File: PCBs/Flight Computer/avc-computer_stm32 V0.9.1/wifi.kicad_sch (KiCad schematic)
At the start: 1 part, among them J3 ESP_01_Socket

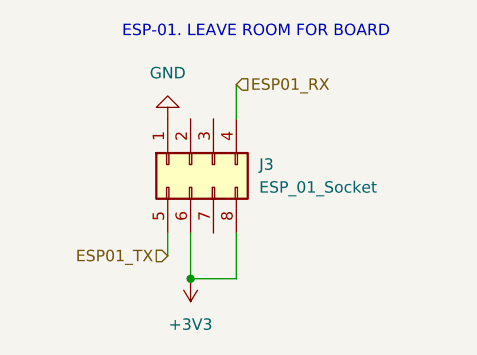
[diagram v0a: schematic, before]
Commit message: Fixed all issues except for 5v buck inductor heating
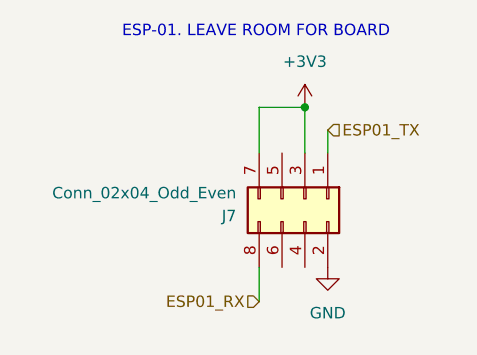
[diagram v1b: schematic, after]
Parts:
- removed J3: ESP_01_Socket, Connector_PinHeader_2.54mm:PinHeader_2x04_P2.54mm_Vertical, symbol Connector_Generic:Conn_02x04_Top_Bottom
- added J7: Conn_02x04_Odd_Even, Connector_PinHeader_2.54mm:PinHeader_2x04_P2.54mm_Vertical, symbol Connector_Generic:Conn_02x04_Odd_Even
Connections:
- net +3V3: now also J7.3 (Pin_3), J7.7 (Pin_7)
- net ESP01_RX: now also J7.8 (Pin_8)
- net ESP01_TX: now also J7.1 (Pin_1)
- net GND: now also J7.2 (Pin_2)
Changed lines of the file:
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@@
-(kicad_sch (version 20211123) (generator eeschema)
+(kicad_sch (version 20230121) (generator eeschema)
   (paper "A4")
-  (junction (at 124.46 74.93) (diameter 0) (color 0 0 0 0)
+  (junction (at 137.16 55.88) (diameter 0) (color 0 0 0 0)
   )
-  (wire (pts (xy 121.92 69.85) (xy 121.92 72.39))
-    (stroke (width 0) (type default) (color 0 0 0 0))
+  (wire (pts (xy 132.08 77.47) (xy 132.08 73.66))
+    (stroke (width 0) (type default))
   )
-  (wire (pts (xy 129.54 74.93) (xy 129.54 69.85))
-    (stroke (width 0) (type default) (color 0 0 0 0))
+  (wire (pts (xy 137.16 55.88) (xy 137.16 60.96))
+    (stroke (width 0) (type default))
   )
-  (wire (pts (xy 124.46 74.93) (xy 124.46 69.85))
-    (stroke (width 0) (type default) (color 0 0 0 0))
+  (wire (pts (xy 139.7 60.96) (xy 139.7 58.42))
+    (stroke (width 0) (type default))
   )
-  (wire (pts (xy 129.54 74.93) (xy 124.46 74.93))
-    (stroke (width 0) (type default) (color 0 0 0 0))
+  (wire (pts (xy 132.08 55.88) (xy 137.16 55.88))
+    (stroke (width 0) (type default))
   )
-  (wire (pts (xy 129.54 53.34) (xy 129.54 57.15))
-    (stroke (width 0) (type default) (color 0 0 0 0))
+  (wire (pts (xy 132.08 55.88) (xy 132.08 60.96))
+    (stroke (width 0) (type default))
   )
   (text "ESP-01. LEAVE ROOM FOR BOARD" (at 116.84 48.26 0)
     (effects (font (size 1.27 1.27)) (justify left bottom))
   )
-  (hierarchical_label "ESP01_RX" (shape input) (at 129.54 53.34 0)
+  (hierarchical_label "ESP01_TX" (shape input) (at 139.7 58.42 0) (fields_autoplaced)
     (effects (font (size 1.27 1.27)) (justify left))
   )
-  (hierarchical_label "ESP01_TX" (shape input) (at 121.92 72.39 180)
+  (hierarchical_label "ESP01_RX" (shape input) (at 132.08 77.47 180) (fields_autoplaced)
     (effects (font (size 1.27 1.27)) (justify right))
   )
-  (symbol (lib_id "power:+3V3") (at 124.46 74.93 0) (mirror x) (unit 1)
-    (in_bom yes) (on_board yes) (fields_autoplaced)
-    (property "Reference" "#PWR0152" (id 0) (at 124.46 71.12 0)
+  (symbol (lib_id "power:GND") (at 139.7 73.66 0) (mirror y) (unit 1)
+    (in_bom yes) (on_board yes) (dnp no) (fields_autoplaced)
+    (property "Reference" "#PWR02" (at 139.7 80.01 0)
       (effects (font (size 1.27 1.27)) hide)
     )
-    (property "Value" "+3V3" (id 1) (at 124.46 80.01 0))
-    (property "Footprint" "" (id 2) (at 124.46 74.93 0)
+    (property "Value" "GND" (at 139.7 78.74 0)
+      (effects (font (size 1.27 1.27)))
+    )
+    (property "Footprint" "" (at 139.7 73.66 0)
       (effects (font (size 1.27 1.27)) hide)
     )
-    (property "Datasheet" "" (id 3) (at 124.46 74.93 0)
+    (property "Datasheet" "" (at 139.7 73.66 0)
       (effects (font (size 1.27 1.27)) hide)
     )
     (pin "1")
+    (instances
+      (project "avc-computer"
+        (path "/e63e39d7-6ac0-4ffd-8aa3-1841a4541b55/144aa036-8f15-4412-804a-63168122b29e"
+          (reference "#PWR02") (unit 1)
+        )
+      )
+    )
   )
-  (symbol (lib_id "power:GND") (at 121.92 57.15 0) (mirror x) (unit 1)
-    (in_bom yes) (on_board yes) (fields_autoplaced)
-    (property "Reference" "#PWR0151" (id 0) (at 121.92 50.8 0)
+  (symbol (lib_id "Connector_Generic:Conn_02x04_Odd_Even") (at 137.16 66.04 270) (unit 1)
+    (in_bom yes) (on_board yes) (dnp no) (fields_autoplaced)
+    (property "Reference" "J7" (at 129.54 67.945 90)
+      (effects (font (size 1.27 1.27)) (justify right))
+    )
+    (property "Value" "Conn_02x04_Odd_Even" (at 129.54 65.405 90)
+      (effects (font (size 1.27 1.27)) (justify right))
+    )
+    (property "Footprint" "Connector_PinHeader_2.54mm:PinHeader_2x04_P2.54mm_Vertical" (at 137.16 66.04 0)
       (effects (font (size 1.27 1.27)) hide)
     )
-    (property "Value" "GND" (id 1) (at 121.92 52.07 0))
-    (property "Footprint" "" (id 2) (at 121.92 57.15 0)
-      (effects (font (size 1.27 1.27)) hide)
-    )
-    (property "Datasheet" "" (id 3) (at 121.92 57.15 0)
-      (effects (font (size 1.27 1.27)) hide)
-    )
-    (pin "1")
-  )
-  (symbol (lib_id "Connector_Generic:Conn_02x04_Top_Bottom") (at 124.46 62.23 90) (mirror x) (unit 1)
-    (in_bom yes) (on_board yes) (fields_autoplaced)
-    (property "Reference" "J3" (id 0) (at 132.08 62.2299 90)
-      (effects (font (size 1.27 1.27)) (justify right))
-    )
-    (property "Value" "ESP_01_Socket" (id 1) (at 132.08 64.7699 90)
-      (effects (font (size 1.27 1.27)) (justify right))
-    )
-    (property "Footprint" "Connector_PinHeader_2.54mm:PinHeader_2x04_P2.54mm_Vertical" (id 2) (at 124.46 62.23 0)
-      (effects (font (size 1.27 1.27)) hide)
-    )
-    (property "Datasheet" "~" (id 3) (at 124.46 62.23 0)
+    (property "Datasheet" "~" (at 137.16 66.04 0)
       (effects (font (size 1.27 1.27)) hide)
     )
@@
     (pin "7")
     (pin "8")
+    (instances
+      (project "avc-computer"
+        (path "/e63e39d7-6ac0-4ffd-8aa3-1841a4541b55/144aa036-8f15-4412-804a-63168122b29e"
+          (reference "J7") (unit 1)
+        )
+      )
+    )
+  )
+  (symbol (lib_id "power:+3V3") (at 137.16 55.88 0) (mirror y) (unit 1)
+    (in_bom yes) (on_board yes) (dnp no) (fields_autoplaced)
+    (property "Reference" "#PWR01" (at 137.16 59.69 0)
+      (effects (font (size 1.27 1.27)) hide)
+    )
+    (property "Value" "+3V3" (at 137.16 50.8 0)
+      (effects (font (size 1.27 1.27)))
+    )
+    (property "Footprint" "" (at 137.16 55.88 0)
+      (effects (font (size 1.27 1.27)) hide)
+    )
+    (property "Datasheet" "" (at 137.16 55.88 0)
+      (effects (font (size 1.27 1.27)) hide)
+    )
+    (pin "1")
+    (instances
+      (project "avc-computer"
+        (path "/e63e39d7-6ac0-4ffd-8aa3-1841a4541b55/144aa036-8f15-4412-804a-63168122b29e"
+          (reference "#PWR01") (unit 1)
+        )
+      )
+    )
   )
 )
